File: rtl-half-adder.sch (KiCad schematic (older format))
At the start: 37 parts, among them Q1 Q_NPN_EBC, Q10 Q_NPN_EBC, Q11 Q_NPN_EBC, Q12 Q_NPN_EBC, Q13 Q_NPN_EBC, Q2 Q_NPN_EBC, Q3 Q_NPN_EBC, Q4 Q_NPN_EBC, Q5 Q_NPN_EBC, Q6 Q_NPN_EBC, Q7 Q_NPN_EBC, Q8 Q_NPN_EBC, Q9 Q_NPN_EBC, SW1 SW_DIP_x02

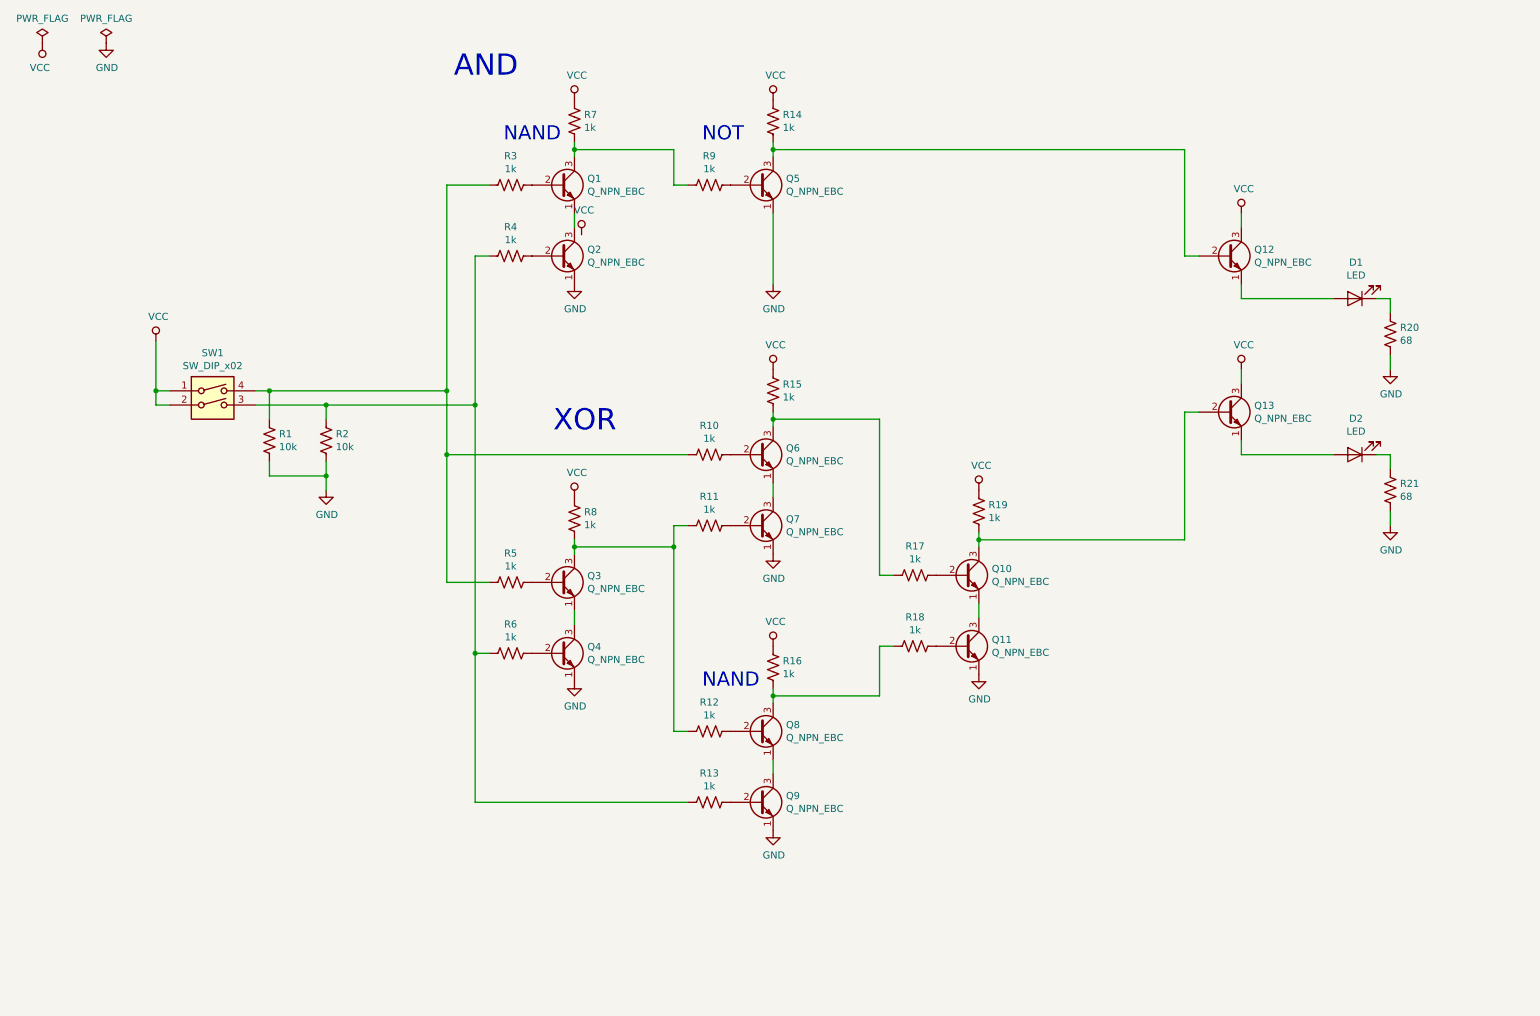
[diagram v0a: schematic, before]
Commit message: through hole components and silk screen done
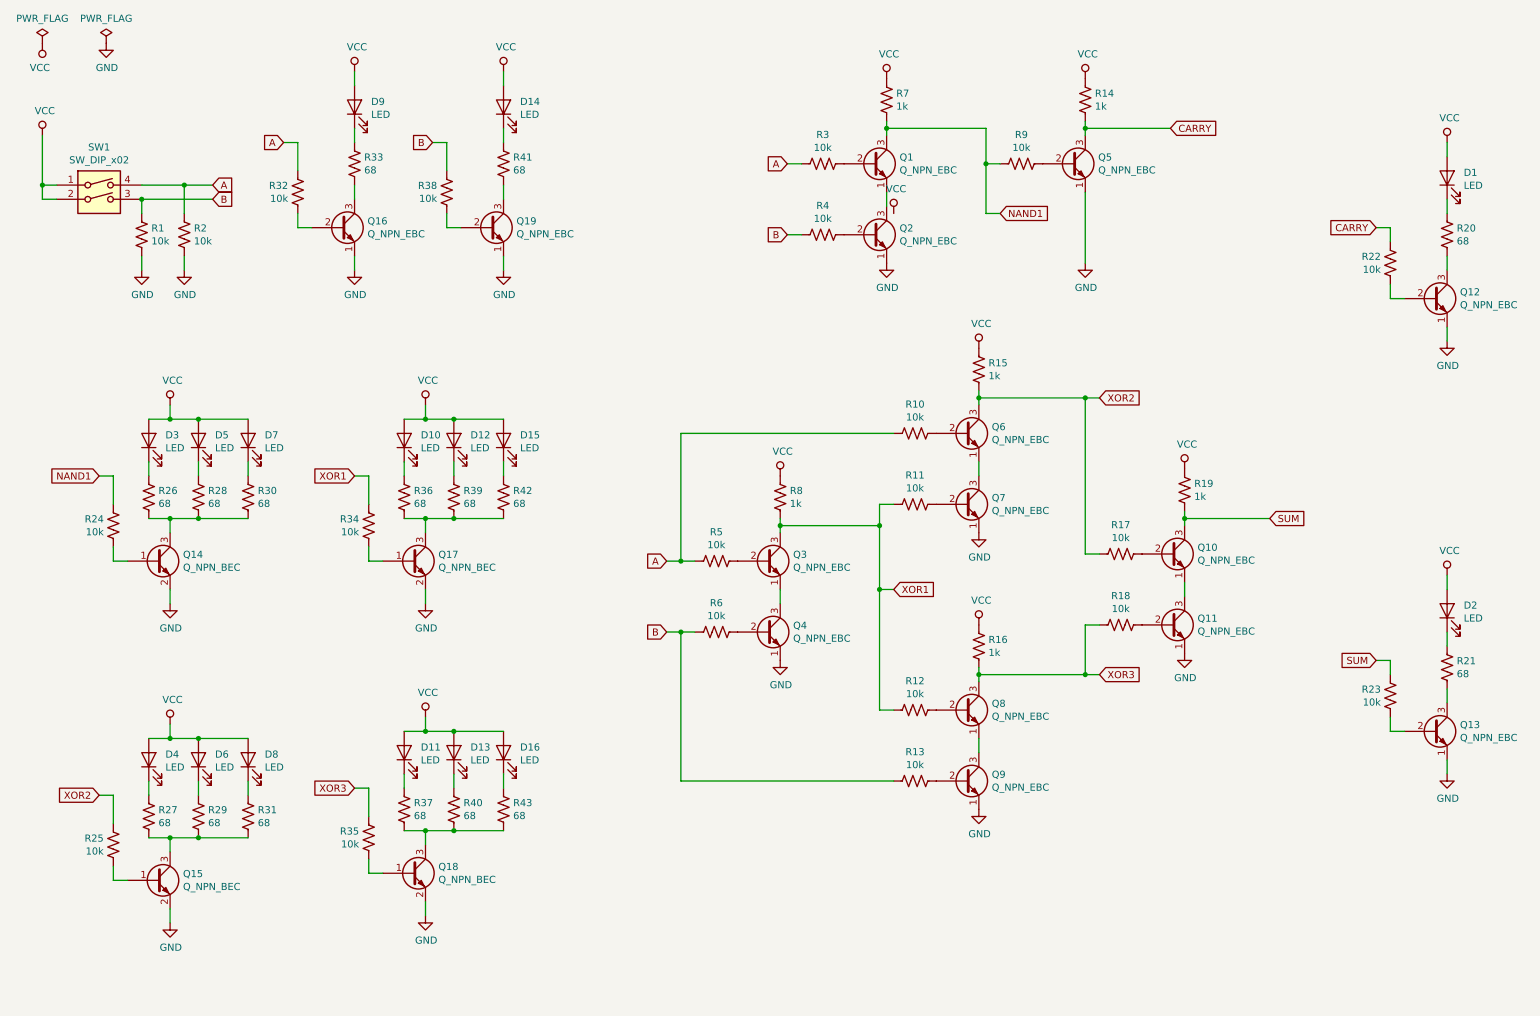
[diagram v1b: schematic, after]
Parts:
- added D10, D11, D12, D13, D15, D16, D3, D4, D5, D6, D7, D8: LED, LED_SMD:LED_0805_2012Metric_Pad1.15x1.40mm_HandSolder, symbol Device:LED
- added D14, D9: LED, LED_THT:LED_D5.0mm, symbol Device:LED
- added Q14, Q15, Q17, Q18: Q_NPN_BEC, Package_TO_SOT_SMD:SOT-23_Handsoldering, symbol Device:Q_NPN_BEC
- added Q16, Q19: Q_NPN_EBC, Package_TO_SOT_THT:TO-92_HandSolder, symbol Device:Q_NPN_EBC
- added R22, R23, R32, R38: 10k, Resistor_THT:R_Axial_DIN0207_L6.3mm_D2.5mm_P7.62mm_Horizontal, symbol Device:R_US
- added R24, R25, R34, R35: 10k, Resistor_SMD:R_0805_2012Metric_Pad1.15x1.40mm_HandSolder, symbol Device:R_US
- added R26, R27, R28, R29, R30, R31, R36, R37, R39, R40, R42, R43: 68, Resistor_SMD:R_0805_2012Metric_Pad1.15x1.40mm_HandSolder, symbol Device:R_US
- added R33, R41: 68, Resistor_THT:R_Axial_DIN0207_L6.3mm_D2.5mm_P7.62mm_Horizontal, symbol Device:R_US
- R10, R11, R12, R13, R17, R18, R3, R4, R5, R6, R9: value 1k -> 10k
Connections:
- net GND: now also Q12.1 (E), Q13.1 (E), Q14.2 (E), Q15.2 (E), Q16.1 (E), Q17.2 (E), Q18.2 (E), Q19.1 (E); no longer R20.2, R21.2
- net VCC: now also D1.2 (A), D2.2 (A), D10.2 (A), D11.2 (A), D12.2 (A), D13.2 (A), D14.2 (A), D15.2 (A), D16.2 (A), D3.2 (A), D4.2 (A), D5.2 (A), D6.2 (A), D7.2 (A), D8.2 (A), D9.2 (A); no longer Q12.3 (C), Q13.3 (C)
- net B: now reaches R13.2, R4.2, R6.2, SW1.3
- net B: now also R1.1, R38.2; no longer R2.1
- net A: now reaches R10.2, R3.2, R5.2, SW1.4
- net A: now also R2.1, R32.2; no longer R1.1
- net XOR1: now reaches Q3.3 (C), R11.2, R12.2, R8.2
- net XOR1: now also R34.2
- net XOR2: now reaches Q6.3 (C), R15.2, R17.2
- net XOR2: now also R25.2
- net XOR3: now reaches Q8.3 (C), R16.2, R18.2
- net XOR3: now also R35.2
- net SUM: now reaches Q10.3 (C), R19.2
- net SUM: now also R23.2; no longer Q13.2 (B)
- net NAND1: now reaches Q1.3 (C), R7.2, R9.2
- net NAND1: now also R24.2
- net CARRY: now reaches Q5.3 (C), R14.2
- net CARRY: now also R22.2; no longer Q12.2 (B)
- new net: Q13.2 (B), R23.1
- new net: Q12.2 (B), R22.1
- new net: Q12.3 (C), R20.2
- new net: Q13.3 (C), R21.2
- new net: D9.1 (K), R33.1
- new net: Q16.3 (C), R33.2
- new net: Q16.2 (B), R32.1
- new net: D14.1 (K), R41.1
- new net: Q19.3 (C), R41.2
- new net: Q19.2 (B), R38.1
- new net: D3.1 (K), R26.1
- new net: Q14.3 (C), R26.2, R28.2, R30.2
- new net: Q14.1 (B), R24.1
- new net: D5.1 (K), R28.1
- new net: D7.1 (K), R30.1
- new net: D4.1 (K), R27.1
- new net: Q15.3 (C), R27.2, R29.2, R31.2
- new net: Q15.1 (B), R25.1
- new net: D6.1 (K), R29.1
- new net: D8.1 (K), R31.1
- new net: D11.1 (K), R37.1
- new net: Q18.3 (C), R37.2, R40.2, R43.2
- new net: Q18.1 (B), R35.1
- new net: D13.1 (K), R40.1
- new net: D16.1 (K), R43.1
- new net: D10.1 (K), R36.1
- new net: Q17.3 (C), R36.2, R39.2, R42.2
- new net: Q17.1 (B), R34.1
- new net: D12.1 (K), R39.1
- new net: D15.1 (K), R42.1
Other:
- note removed: "AND"
- note removed: "NAND"
- note removed: "NOT"
- note removed: "XOR"
- moved on the sheet: D1, D2, Q1, Q10, Q11, Q12, Q13, Q2, Q3, Q4, Q5, Q6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

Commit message: update footprints for smd leds
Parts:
- D10, D11, D12, D13, D15, D16, D3, D4, D5, D6, D7, D8: footprint LED_SMD:LED_0805_2012Metric_Pad1.15x1.40mm_HandSolder -> --Project:LED_1206_3216Metric_ReverseMount_Hole1.8x2.4mm; Link (none) -> http://www.inolux-corp.com/datasheet/SMDLED/Mono%20Color%20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
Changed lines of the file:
@@
 F 0 "D3" V 1488 3433 50  0000 R CNN
 F 1 "LED" V 1397 3433 50  0000 R CNN
-F 2 "LED_SMD:LED_0805_2012Metric_Pad1.15x1.40mm_HandSolder" H 1450 3550 50  0001 C CNN
-F 3 "~" H 1450 3550 50  0001 C CNN
+F 2 "--Project:LED_1206_3216Metric_ReverseMount_Hole1.8x2.4mm" H 1450 3550 50  0001 C CNN
+F 3 "https://www.mouser.com/ProductDetail/IN-S124BRUW" H 1450 3550 50  0001 C CNN
+F 4 "http://www.inolux-corp.com/datasheet/SMDLED/Mono%20Color%20Reverse%20Mount/IN-S124BR%20Series_V1.0.pdf" H 0   0   50  0001 C CNN "Link"
 	1    1450 3550
 	0    -1   -1   0
@@
 F 0 "D5" V 1838 3433 50  0000 R CNN
 F 1 "LED" V 1747 3433 50  0000 R CNN
-F 2 "LED_SMD:LED_0805_2012Metric_Pad1.15x1.40mm_HandSolder" H 1800 3550 50  0001 C CNN
-F 3 "~" H 1800 3550 50  0001 C CNN
+F 2 "--Project:LED_1206_3216Metric_ReverseMount_Hole1.8x2.4mm" H 1800 3550 50  0001 C CNN
+F 3 "https://www.mouser.com/ProductDetail/IN-S124BRUW" H 1800 3550 50  0001 C CNN
+F 4 "http://www.inolux-corp.com/datasheet/SMDLED/Mono%20Color%20Reverse%20Mount/IN-S124BR%20Series_V1.0.pdf" H 0   0   50  0001 C CNN "Link"
 	1    1800 3550
 	0    -1   -1   0
@@
 F 0 "D7" V 2188 3433 50  0000 R CNN
 F 1 "LED" V 2097 3433 50  0000 R CNN
-F 2 "LED_SMD:LED_0805_2012Metric_Pad1.15x1.40mm_HandSolder" H 2150 3550 50  0001 C CNN
-F 3 "~" H 2150 3550 50  0001 C CNN
+F 2 "--Project:LED_1206_3216Metric_ReverseMount_Hole1.8x2.4mm" H 2150 3550 50  0001 C CNN
+F 3 "https://www.mouser.com/ProductDetail/IN-S124BRUW" H 2150 3550 50  0001 C CNN
+F 4 "http://www.inolux-corp.com/datasheet/SMDLED/Mono%20Color%20Reverse%20Mount/IN-S124BR%20Series_V1.0.pdf" H 0   0   50  0001 C CNN "Link"
 	1    2150 3550
 	0    -1   -1   0
@@
 F 0 "D4" V 1488 5683 50  0000 R CNN
 F 1 "LED" V 1397 5683 50  0000 R CNN
-F 2 "LED_SMD:LED_0805_2012Metric_Pad1.15x1.40mm_HandSolder" H 1450 5800 50  0001 C CNN
-F 3 "~" H 1450 5800 50  0001 C CNN
+F 2 "--Project:LED_1206_3216Metric_ReverseMount_Hole1.8x2.4mm" H 1450 5800 50  0001 C CNN
+F 3 "https://www.mouser.com/ProductDetail/IN-S124BRUW" H 1450 5800 50  0001 C CNN
+F 4 "http://www.inolux-corp.com/datasheet/SMDLED/Mono%20Color%20Reverse%20Mount/IN-S124BR%20Series_V1.0.pdf" H 0   0   50  0001 C CNN "Link"
 	1    1450 5800
 	0    -1   -1   0
@@
 F 0 "D6" V 1838 5683 50  0000 R CNN
 F 1 "LED" V 1747 5683 50  0000 R CNN
-F 2 "LED_SMD:LED_0805_2012Metric_Pad1.15x1.40mm_HandSolder" H 1800 5800 50  0001 C CNN
-F 3 "~" H 1800 5800 50  0001 C CNN
+F 2 "--Project:LED_1206_3216Metric_ReverseMount_Hole1.8x2.4mm" H 1800 5800 50  0001 C CNN
+F 3 "https://www.mouser.com/ProductDetail/IN-S124BRUW" H 1800 5800 50  0001 C CNN
+F 4 "http://www.inolux-corp.com/datasheet/SMDLED/Mono%20Color%20Reverse%20Mount/IN-S124BR%20Series_V1.0.pdf" H 0   0   50  0001 C CNN "Link"
 	1    1800 5800
 	0    -1   -1   0
@@
 F 0 "D8" V 2188 5683 50  0000 R CNN
 F 1 "LED" V 2097 5683 50  0000 R CNN
-F 2 "LED_SMD:LED_0805_2012Metric_Pad1.15x1.40mm_HandSolder" H 2150 5800 50  0001 C CNN
-F 3 "~" H 2150 5800 50  0001 C CNN
+F 2 "--Project:LED_1206_3216Metric_ReverseMount_Hole1.8x2.4mm" H 2150 5800 50  0001 C CNN
+F 3 "https://www.mouser.com/ProductDetail/IN-S124BRUW" H 2150 5800 50  0001 C CNN
+F 4 "http://www.inolux-corp.com/datasheet/SMDLED/Mono%20Color%20Reverse%20Mount/IN-S124BR%20Series_V1.0.pdf" H 0   0   50  0001 C CNN "Link"
 	1    2150 5800
 	0    -1   -1   0
@@
 F 0 "D11" V 3288 5633 50  0000 R CNN
 F 1 "LED" V 3197 5633 50  0000 R CNN
-F 2 "LED_SMD:LED_0805_2012Metric_Pad1.15x1.40mm_HandSolder" H 3250 5750 50  0001 C CNN
-F 3 "~" H 3250 5750 50  0001 C CNN
+F 2 "--Project:LED_1206_3216Metric_ReverseMount_Hole1.8x2.4mm" H 3250 5750 50  0001 C CNN
+F 3 "https://www.mouser.com/ProductDetail/IN-S124BRUW" H 3250 5750 50  0001 C CNN
+F 4 "http://www.inolux-corp.com/datasheet/SMDLED/Mono%20Color%20Reverse%20Mount/IN-S124BR%20Series_V1.0.pdf" H 0   0   50  0001 C CNN "Link"
 	1    3250 5750
 	0    -1   -1   0
@@
 F 0 "D13" V 3638 5633 50  0000 R CNN
 F 1 "LED" V 3547 5633 50  0000 R CNN
-F 2 "LED_SMD:LED_0805_2012Metric_Pad1.15x1.40mm_HandSolder" H 3600 5750 50  0001 C CNN
-F 3 "~" H 3600 5750 50  0001 C CNN
+F 2 "--Project:LED_1206_3216Metric_ReverseMount_Hole1.8x2.4mm" H 3600 5750 50  0001 C CNN
+F 3 "https://www.mouser.com/ProductDetail/IN-S124BRUW" H 3600 5750 50  0001 C CNN
+F 4 "http://www.inolux-corp.com/datasheet/SMDLED/Mono%20Color%20Reverse%20Mount/IN-S124BR%20Series_V1.0.pdf" H 0   0   50  0001 C CNN "Link"
 	1    3600 5750
 	0    -1   -1   0
@@
 F 0 "D16" V 3988 5633 50  0000 R CNN
 F 1 "LED" V 3897 5633 50  0000 R CNN
-F 2 "LED_SMD:LED_0805_2012Metric_Pad1.15x1.40mm_HandSolder" H 3950 5750 50  0001 C CNN
-F 3 "~" H 3950 5750 50  0001 C CNN
+F 2 "--Project:LED_1206_3216Metric_ReverseMount_Hole1.8x2.4mm" H 3950 5750 50  0001 C CNN
+F 3 "https://www.mouser.com/ProductDetail/IN-S124BRUW" H 3950 5750 50  0001 C CNN
+F 4 "http://www.inolux-corp.com/datasheet/SMDLED/Mono%20Color%20Reverse%20Mount/IN-S124BR%20Series_V1.0.pdf" H 0   0   50  0001 C CNN "Link"
 	1    3950 5750
 	0    -1   -1   0
@@
 F 0 "D10" V 3288 3433 50  0000 R CNN
 F 1 "LED" V 3197 3433 50  0000 R CNN
-F 2 "LED_SMD:LED_0805_2012Metric_Pad1.15x1.40mm_HandSolder" H 3250 3550 50  0001 C CNN
-F 3 "~" H 3250 3550 50  0001 C CNN
+F 2 "--Project:LED_1206_3216Metric_ReverseMount_Hole1.8x2.4mm" H 3250 3550 50  0001 C CNN
+F 3 "https://www.mouser.com/ProductDetail/IN-S124BRUW" H 3250 3550 50  0001 C CNN
+F 4 "http://www.inolux-corp.com/datasheet/SMDLED/Mono%20Color%20Reverse%20Mount/IN-S124BR%20Series_V1.0.pdf" H 0   0   50  0001 C CNN "Link"
 	1    3250 3550
 	0    -1   -1   0
@@
 F 0 "D12" V 3638 3433 50  0000 R CNN
 F 1 "LED" V 3547 3433 50  0000 R CNN
-F 2 "LED_SMD:LED_0805_2012Metric_Pad1.15x1.40mm_HandSolder" H 3600 3550 50  0001 C CNN
-F 3 "~" H 3600 3550 50  0001 C CNN
+F 2 "--Project:LED_1206_3216Metric_ReverseMount_Hole1.8x2.4mm" H 3600 3550 50  0001 C CNN
+F 3 "https://www.mouser.com/ProductDetail/IN-S124BRUW" H 3600 3550 50  0001 C CNN
+F 4 "http://www.inolux-corp.com/datasheet/SMDLED/Mono%20Color%20Reverse%20Mount/IN-S124BR%20Series_V1.0.pdf" H 0   0   50  0001 C CNN "Link"
 	1    3600 3550
 	0    -1   -1   0
@@
 F 0 "D15" V 3988 3433 50  0000 R CNN
 F 1 "LED" V 3897 3433 50  0000 R CNN
-F 2 "LED_SMD:LED_0805_2012Metric_Pad1.15x1.40mm_HandSolder" H 3950 3550 50  0001 C CNN
-F 3 "~" H 3950 3550 50  0001 C CNN
+F 2 "--Project:LED_1206_3216Metric_ReverseMount_Hole1.8x2.4mm" H 3950 3550 50  0001 C CNN
+F 3 "https://www.mouser.com/ProductDetail/IN-S124BRUW" H 3950 3550 50  0001 C CNN
+F 4 "http://www.inolux-corp.com/datasheet/SMDLED/Mono%20Color%20Reverse%20Mount/IN-S124BR%20Series_V1.0.pdf" H 0   0   50  0001 C CNN "Link"
 	1    3950 3550
 	0    -1   -1   0

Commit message: inter gate led layout done
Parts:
- removed D16, D7, D8: LED, --Project:LED_1206_3216Metric_ReverseMount_Hole1.8x2.4mm, symbol Device:LED
- removed R30, R31, R43: 68, Resistor_SMD:R_0805_2012Metric_Pad1.15x1.40mm_HandSolder, symbol Device:R_US
- added BT?: Battery_Cell, symbol Device:Battery_Cell
- added SW?: SW_SPST, symbol Switch:SW_SPST
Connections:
- net GND: now also BT?.2 (-)
- net VCC: now also SW?.1 (A)
- new net: BT?.1 (+), SW?.2 (B)
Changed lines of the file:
@@
 Wire Wire Line
 	1800 3800 1800 3700
-$Comp
-L Device:LED D7
-U 1 1 5D05623B
-P 2150 3550
-F 0 "D7" V 2188 3433 50  0000 R CNN
-F 1 "LED" V 2097 3433 50  0000 R CNN
-F 2 "--Project:LED_1206_3216Metric_ReverseMount_Hole1.8x2.4mm" H 2150 3550 50  0001 C CNN
-F 3 "https://www.mouser.com/ProductDetail/IN-S124BRUW" H 2150 3550 50  0001 C CNN
-F 4 "http://www.inolux-corp.com/datasheet/SMDLED/Mono%20Color%20Reverse%20Mount/IN-S124BR%20Series_V1.0.pdf" H 0   0   50  0001 C CNN "Link"
-	1    2150 3550
-	0    -1   -1   0
-$EndComp
-$Comp
-L Device:R_US R30
-U 1 1 5D056242
-P 2150 3950
-F 0 "R30" H 2218 3996 50  0000 L CNN
-F 1 "68" H 2218 3905 50  0000 L CNN
-F 2 "Resistor_SMD:R_0805_2012Metric_Pad1.15x1.40mm_HandSolder" V 2190 3940 50  0001 C CNN
-F 3 "~" H 2150 3950 50  0001 C CNN
-	1    2150 3950
-	1    0    0    -1
-$EndComp
-Wire Wire Line
-	2150 3800 2150 3700
 Wire Wire Line
 	1450 4100 1600 4100
@@
 Wire Wire Line
 	1600 4100 1800 4100
-Connection ~ 1800 4100
-Wire Wire Line
-	1800 4100 2150 4100
 Wire Wire Line
 	1450 3400 1600 3400
@@
 Wire Wire Line
 	1600 3400 1800 3400
-Connection ~ 1800 3400
-Wire Wire Line
-	1800 3400 2150 3400
 $Comp
 L Device:LED D4
@@
 Wire Wire Line
 	1800 6050 1800 5950
-$Comp
-L Device:LED D8
-U 1 1 5D060429
-P 2150 5800
-F 0 "D8" V 2188 5683 50  0000 R CNN
-F 1 "LED" V 2097 5683 50  0000 R CNN
-F 2 "--Project:LED_1206_3216Metric_ReverseMount_Hole1.8x2.4mm" H 2150 5800 50  0001 C CNN
-F 3 "https://www.mouser.com/ProductDetail/IN-S124BRUW" H 2150 5800 50  0001 C CNN
-F 4 "http://www.inolux-corp.com/datasheet/SMDLED/Mono%20Color%20Reverse%20Mount/IN-S124BR%20Series_V1.0.pdf" H 0   0   50  0001 C CNN "Link"
-	1    2150 5800
-	0    -1   -1   0
-$EndComp
-$Comp
-L Device:R_US R31
-U 1 1 5D060430
-P 2150 6200
-F 0 "R31" H 2218 6246 50  0000 L CNN
-F 1 "68" H 2218 6155 50  0000 L CNN
-F 2 "Resistor_SMD:R_0805_2012Metric_Pad1.15x1.40mm_HandSolder" V 2190 6190 50  0001 C CNN
-F 3 "~" H 2150 6200 50  0001 C CNN
-	1    2150 6200
-	1    0    0    -1
-$EndComp
-Wire Wire Line
-	2150 6050 2150 5950
 Wire Wire Line
 	1450 6350 1600 6350
@@
 Wire Wire Line
 	1600 6350 1800 6350
-Connection ~ 1800 6350
-Wire Wire Line
-	1800 6350 2150 6350
 Wire Wire Line
 	1450 5650 1600 5650
@@
 Wire Wire Line
 	1600 5650 1800 5650
-Connection ~ 1800 5650
-Wire Wire Line
-	1800 5650 2150 5650
 $Comp
 L Device:LED D11
@@
 Wire Wire Line
 	3600 6000 3600 5900
-$Comp
-L Device:LED D16
-U 1 1 5D06E2BD
-P 3950 5750
-F 0 "D16" V 3988 5633 50  0000 R CNN
-F 1 "LED" V 3897 5633 50  0000 R CNN
-F 2 "--Project:LED_1206_3216Metric_ReverseMount_Hole1.8x2.4mm" H 3950 5750 50  0001 C CNN
-F 3 "https://www.mouser.com/ProductDetail/IN-S124BRUW" H 3950 5750 50  0001 C CNN
-F 4 "http://www.inolux-corp.com/datasheet/SMDLED/Mono%20Color%20Reverse%20Mount/IN-S124BR%20Series_V1.0.pdf" H 0   0   50  0001 C CNN "Link"
-	1    3950 5750
-	0    -1   -1   0
-$EndComp
-$Comp
-L Device:R_US R43
-U 1 1 5D06E2C4
-P 3950 6150
-F 0 "R43" H 4018 6196 50  0000 L CNN
-F 1 "68" H 4018 6105 50  0000 L CNN
-F 2 "Resistor_SMD:R_0805_2012Metric_Pad1.15x1.40mm_HandSolder" V 3990 6140 50  0001 C CNN
-F 3 "~" H 3950 6150 50  0001 C CNN
-	1    3950 6150
-	1    0    0    -1
-$EndComp
-Wire Wire Line
-	3950 6000 3950 5900
 Wire Wire Line
 	3250 6300 3400 6300
@@
 Wire Wire Line
 	3400 6300 3600 6300
-Connection ~ 3600 6300
-Wire Wire Line
-	3600 6300 3950 6300
 Wire Wire Line
 	3250 5600 3400 5600
@@
 Wire Wire Line
 	3400 5600 3600 5600
-Connection ~ 3600 5600
-Wire Wire Line
-	3600 5600 3950 5600
 $Comp
 L Device:LED D10
@@
 	1    0    0    -1
 $EndComp
+$Comp
+L Device:Battery_Cell BT?
+U 1 1 5CFF1130
+P 5500 7100
+F 0 "BT?" H 5618 7196 50  0000 L CNN
+F 1 "Battery_Cell" H 5618 7105 50  0000 L CNN
+F 2 "" V 5500 7160 50  0001 C CNN
+F 3 "~" V 5500 7160 50  0001 C CNN
+	1    5500 7100
+	1    0    0    -1
+$EndComp
+$Comp
+L Switch:SW_SPST SW?
+U 1 1 5CFF1526
+P 5200 6800
+F 0 "SW?" H 5200 7035 50  0000 C CNN
+F 1 "SW_SPST" H 5200 6944 50  0000 C CNN
+F 2 "" H 5200 6800 50  0001 C CNN
+F 3 "" H 5200 6800 50  0001 C CNN
+	1    5200 6800
+	1    0    0    -1
+$EndComp
+$Comp
+L power:VCC #PWR?
+U 1 1 5CFF1688
+P 4900 6700
+F 0 "#PWR?" H 4900 6550 50  0001 C CNN
+F 1 "VCC" H 4917 6873 50  0000 C CNN
+F 2 "" H 4900 6700 50  0001 C CNN
+F 3 "" H 4900 6700 50  0001 C CNN
+	1    4900 6700
+	1    0    0    -1
+$EndComp
+$Comp
+L power:GND #PWR?
+U 1 1 5CFF17CA
+P 5500 7300
+F 0 "#PWR?" H 5500 7050 50  0001 C CNN
+F 1 "GND" H 5505 7127 50  0000 C CNN
+F 2 "" H 5500 7300 50  0001 C CNN
+F 3 "" H 5500 7300 50  0001 C CNN
+	1    5500 7300
+	1    0    0    -1
+$EndComp
+Wire Wire Line
+	4900 6700 4900 6800
+Wire Wire Line
+	4900 6800 5000 6800
+Wire Wire Line
+	5400 6800 5500 6800
+Wire Wire Line
+	5500 6800 5500 6900
+Wire Wire Line
+	5500 7200 5500 7300
 $EndSCHEMATC

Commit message: add battery footprint
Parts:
- BT?: footprint (none) -> --Project:BatteryHolder_CR1220_THT
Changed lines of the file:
@@
 F 0 "BT?" H 5618 7196 50  0000 L CNN
 F 1 "Battery_Cell" H 5618 7105 50  0000 L CNN
-F 2 "" V 5500 7160 50  0001 C CNN
+F 2 "--Project:BatteryHolder_CR1220_THT" V 5500 7160 50  0001 C CNN
 F 3 "~" V 5500 7160 50  0001 C CNN
 	1    5500 7100
